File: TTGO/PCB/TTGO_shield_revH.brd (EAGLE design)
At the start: 113.1 x 113.1 mm, 43 parts

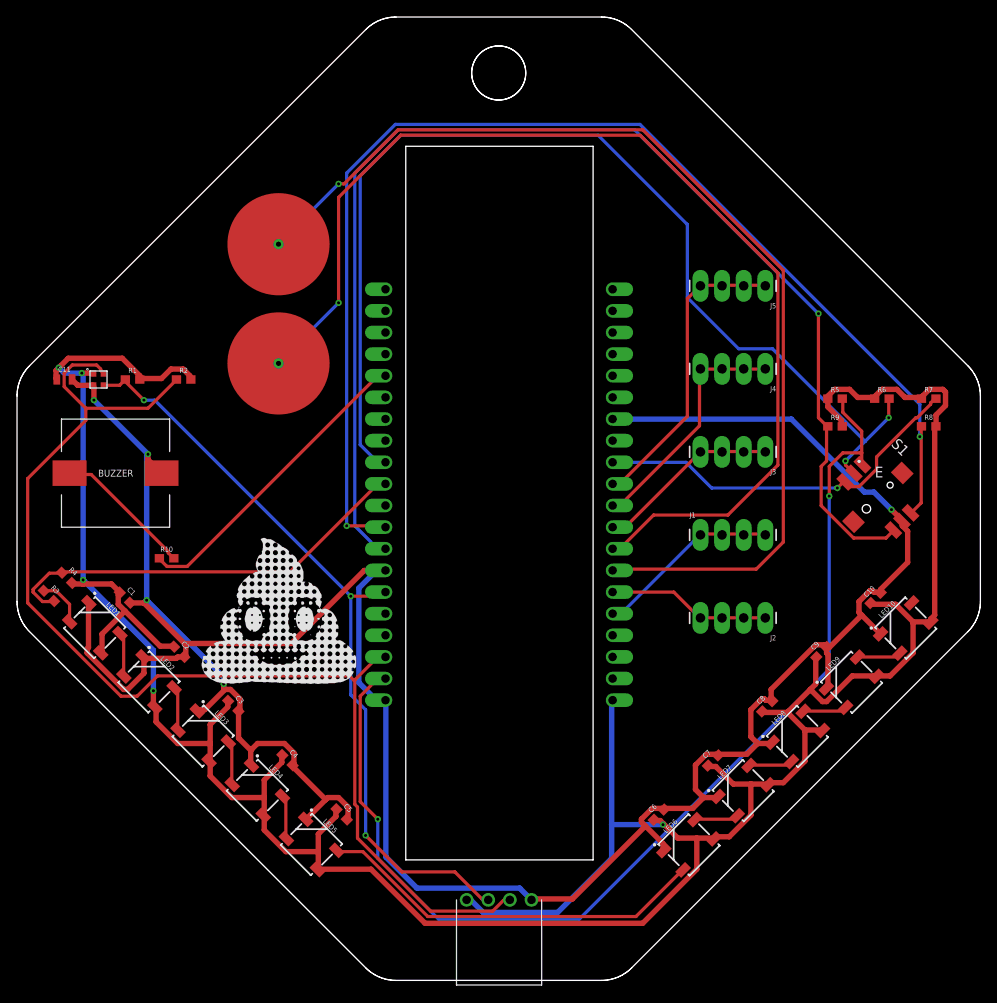
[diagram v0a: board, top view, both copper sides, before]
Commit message: updated capsense buttons to clear oshpark drc
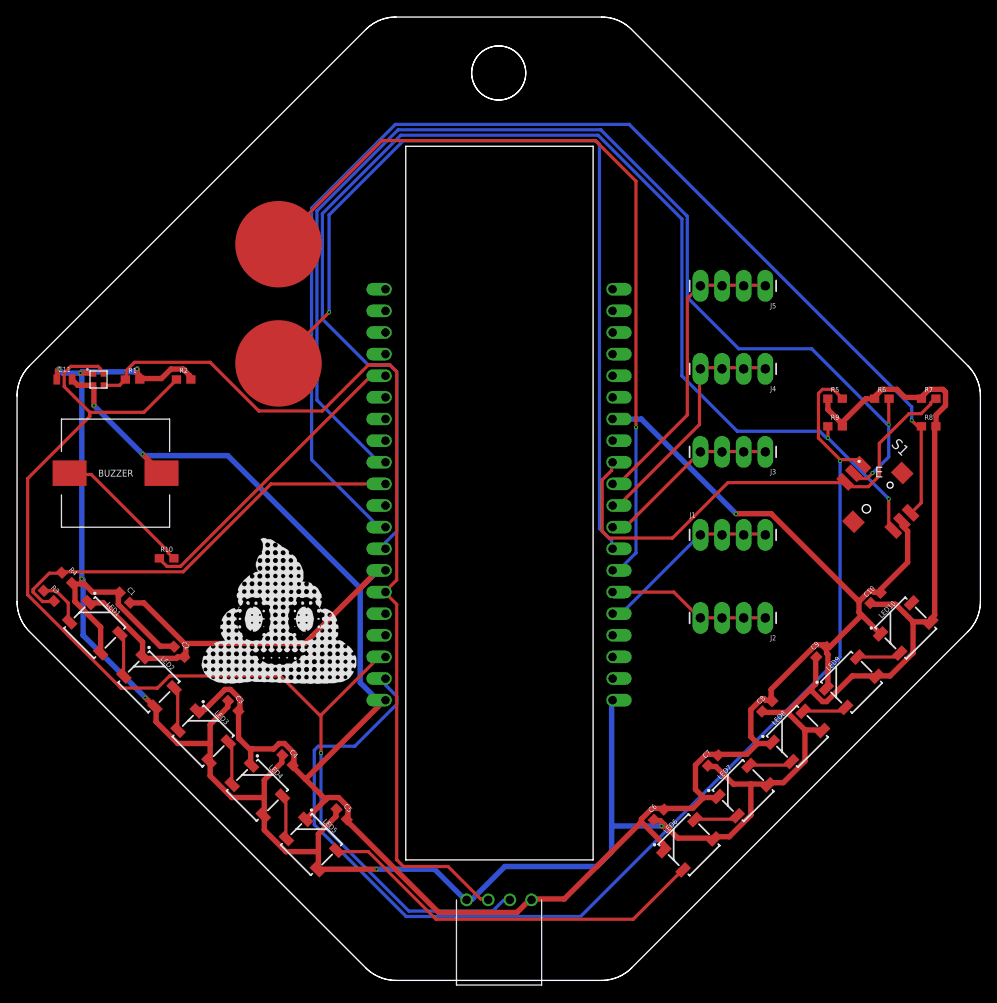
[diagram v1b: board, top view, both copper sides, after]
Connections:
- net 32: now also CAP1.P$1; no longer CAP1.1
- net 33: now also CAP2.P$1; no longer CAP2.1
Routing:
- net VDD: track 365.4 -> 328.3 mm, vias 5 -> 7
- net 32: track 125.1 -> 96.3 mm
- net 33: track 129.8 -> 103.5 mm
- net SDA: track 90.6 -> 112.1 mm, vias 3 -> 0
- net J-UP: track 45.0 -> 57.8 mm, vias 1 -> 0
- net J-RIGHT: track 128.9 -> 141.4 mm, vias 2 -> 1
- net J-PRESS: track 127.9 -> 136.6 mm
- net GND: track 332.5 -> 326.0 mm, vias 5 -> 3
- net J-LEFT: track 145.5 -> 149.1 mm, vias 1 -> 2
- net SCL: track 138.0 -> 139.1 mm, vias 0 -> 1
- net J-DOWN: track 144.0 -> 143.8 mm, vias 2 -> 1
